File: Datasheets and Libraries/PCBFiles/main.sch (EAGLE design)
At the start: 1 part, among them IC1 ATSAMD21E17A-AUT

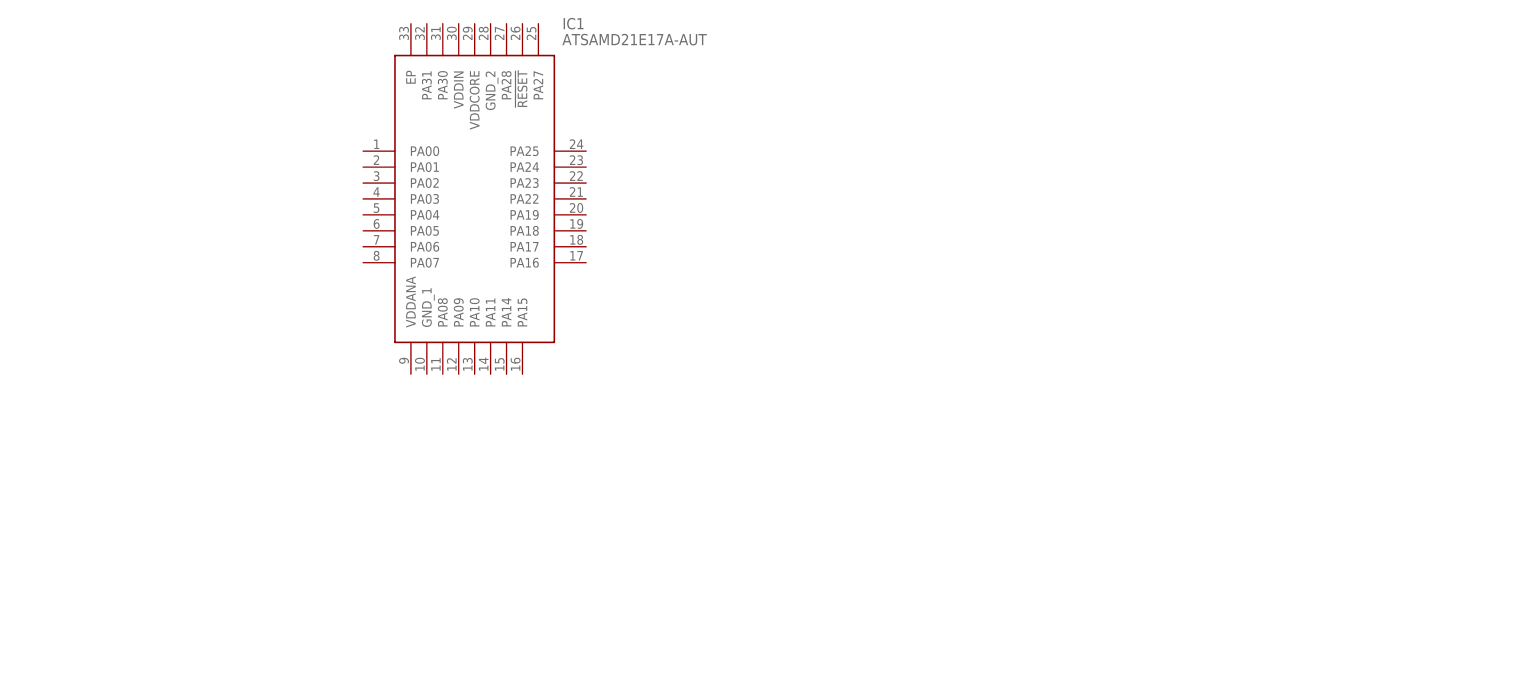
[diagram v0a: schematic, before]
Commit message: Added Custom Footprint for TEMU ST7735
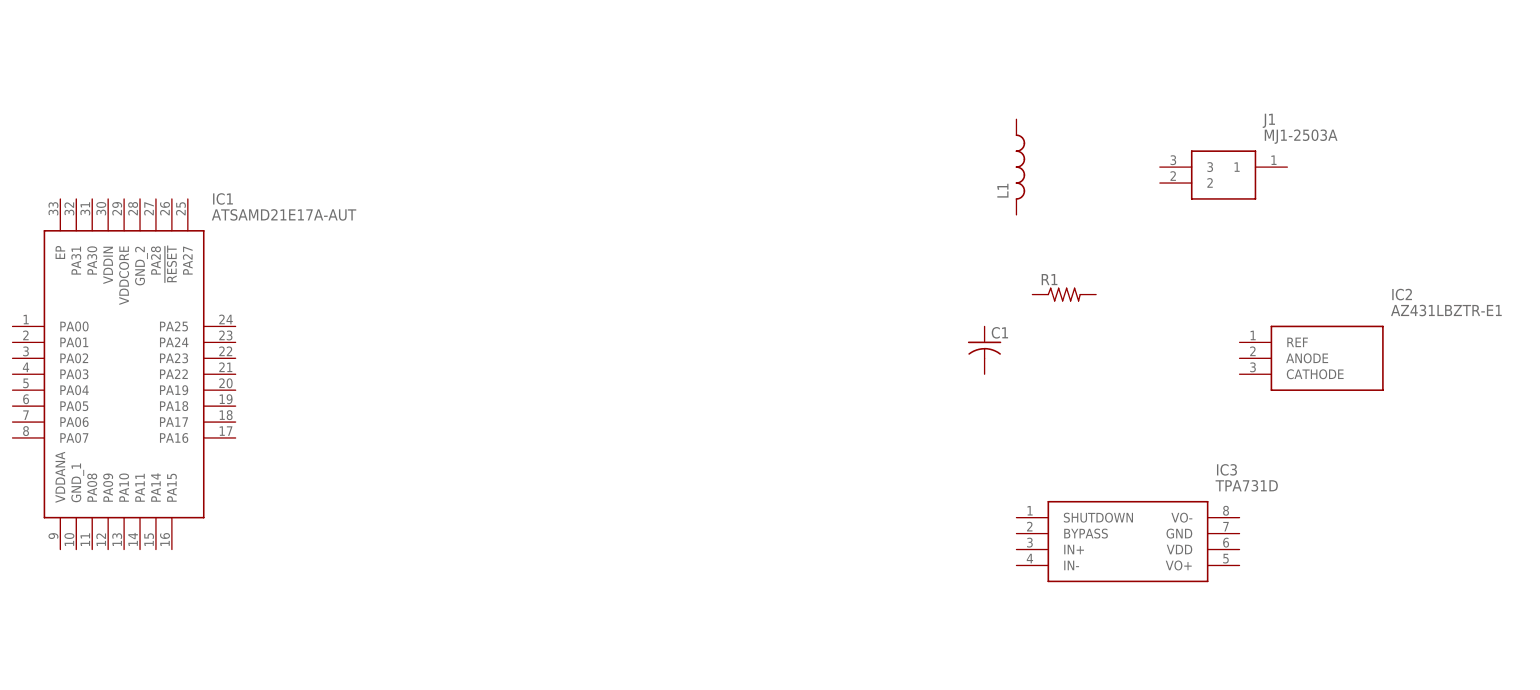
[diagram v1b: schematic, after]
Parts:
- added C1: (no value), rcl:C-US050-024X044
- added IC2: AZ431LBZTR-E1, AZ431LBZTR-E1:AZ431LBZTR-E1
- added IC3: TPA731D, TPA731D:TPA731D
- added J1: MJ1-2503A, MJ1-2503A:MJ1-2503A
- added L1: (no value), rcl:L-US0204/7
- added R1: (no value), rcl:R-US_0204/7
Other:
- moved on the sheet: IC1

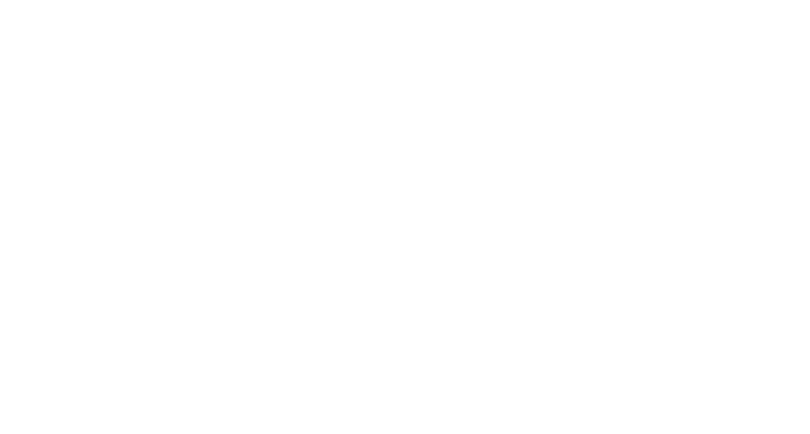
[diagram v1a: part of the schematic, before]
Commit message: Fixed St7735 footprint
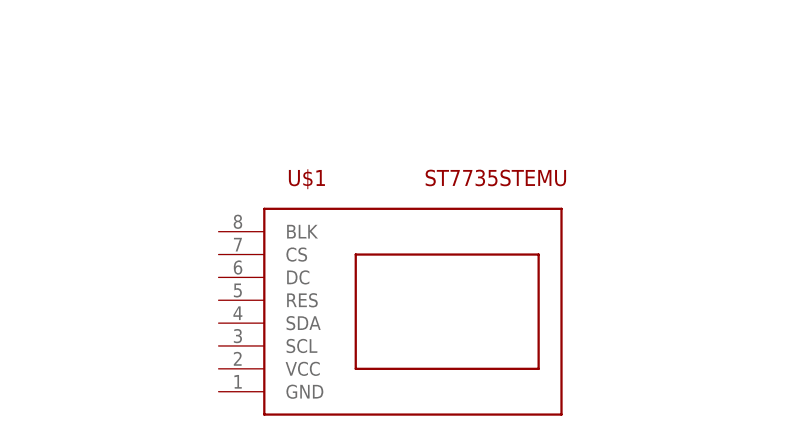
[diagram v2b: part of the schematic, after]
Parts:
- added U$1: ST7735STEMU, ST7735wosd:ST7735STEMU
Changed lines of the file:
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@@
 <part name="L1" library="rcl" library_urn="urn:adsk.eagle:library:334" deviceset="L-US" device="0204/7" package3d_urn="urn:adsk.eagle:package:23498/2"/>
 <part name="R1" library="rcl" library_urn="urn:adsk.eagle:library:334" deviceset="R-US_" device="0204/7" package3d_urn="urn:adsk.eagle:package:23498/2"/>
+<part name="U$1" library="ST7735wosd" deviceset="ST7735STEMU" device=""/>
 </parts>
 <sheets>
@@
 <attribute name="VALUE" x="171.45" y="-71.882" size="1.778" layer="96"/>
 </instance>
+<instance part="U$1" gate="G$1" x="116.84" y="-116.84" smashed="yes">
+<attribute name="NAME" x="99.06" y="-104.14" size="1.778" layer="94"/>
+<attribute name="VALUE" x="114.3" y="-104.14" size="1.778" layer="94"/>
+</instance>
 </instances>
